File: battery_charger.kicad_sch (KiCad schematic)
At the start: 30 parts, among them J8 Conn_01x04, U15 BQ25895RTW, U17 NX3DV42GU, U18 MP3422GG-P

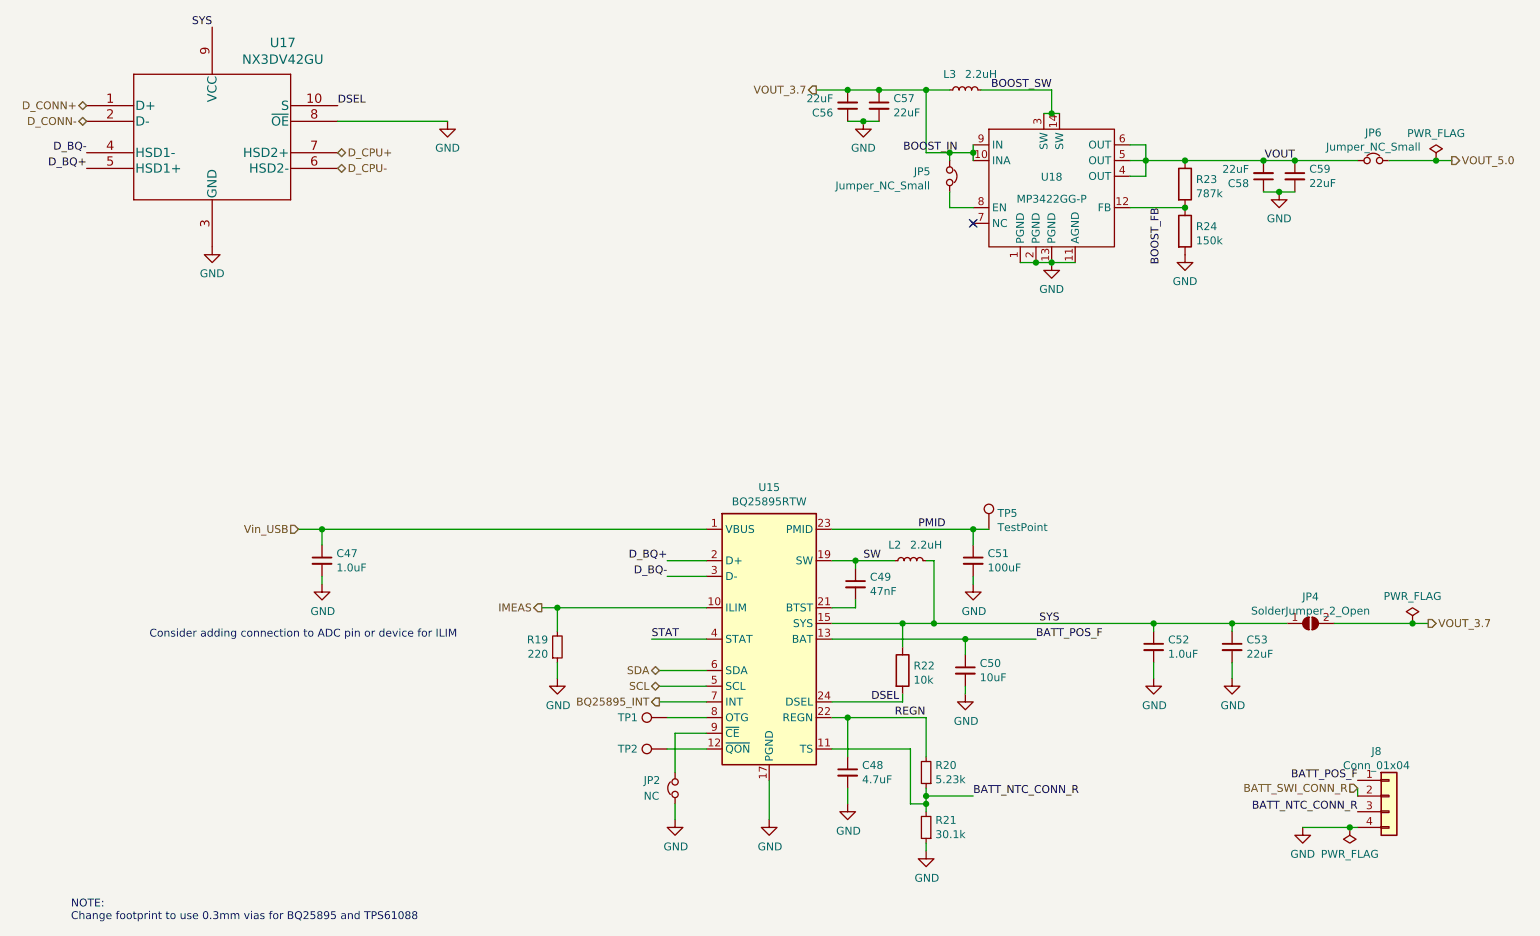
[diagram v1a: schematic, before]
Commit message: Update to Kicad 6.0.0
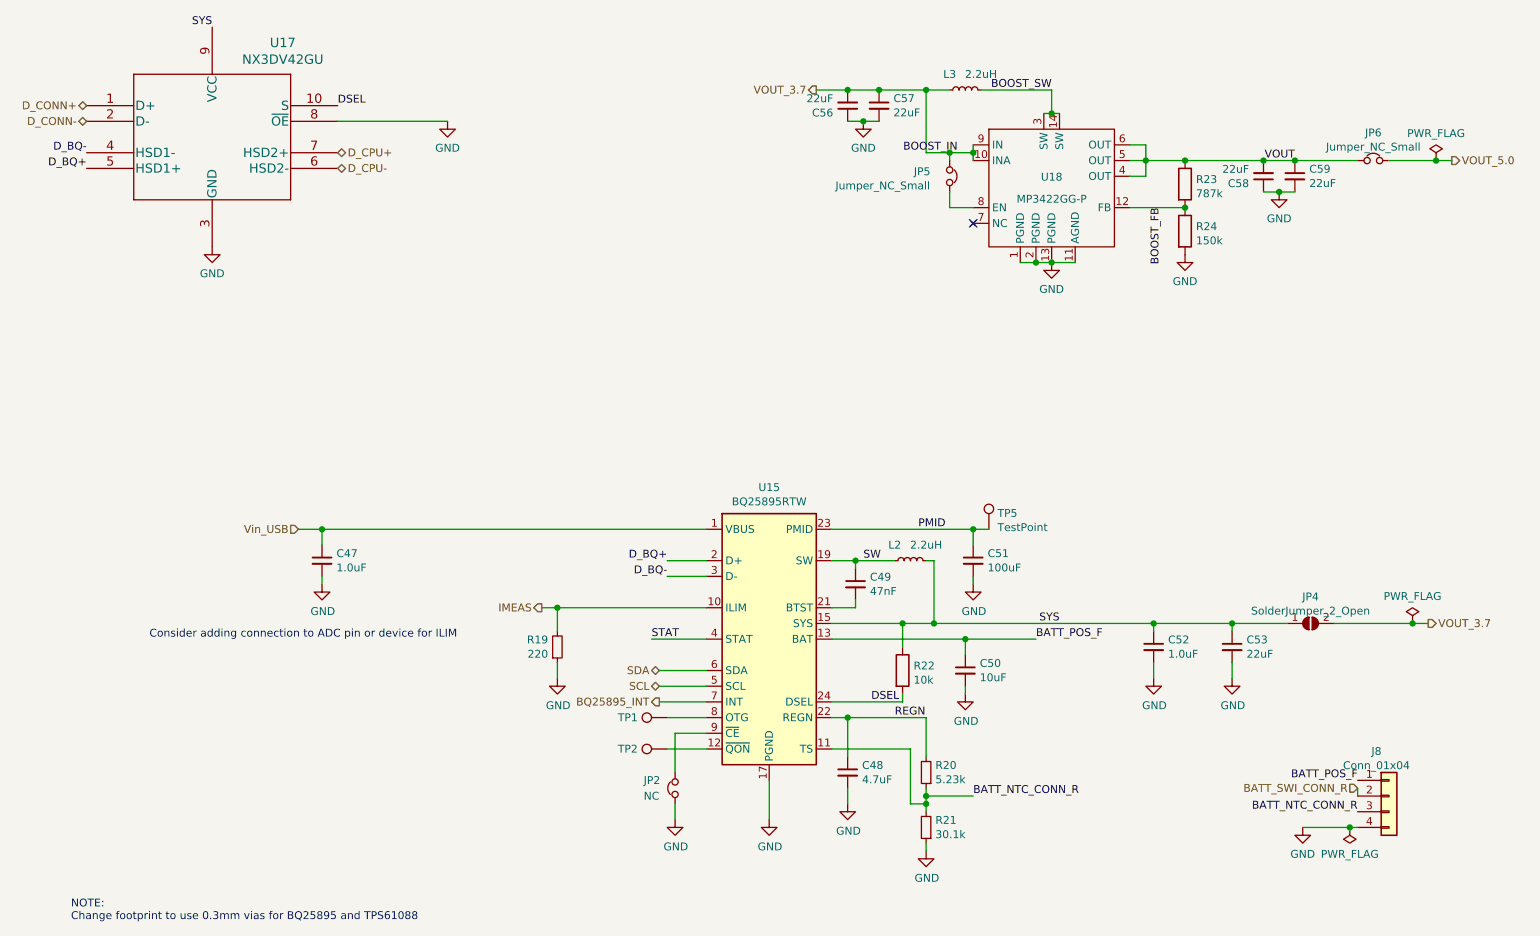
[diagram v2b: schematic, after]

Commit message: Remove tlv320aic3206 and bq25895 and supporting circuitry from schematic; wire up audio/battery connections to Radxa CM3 third connector instead.
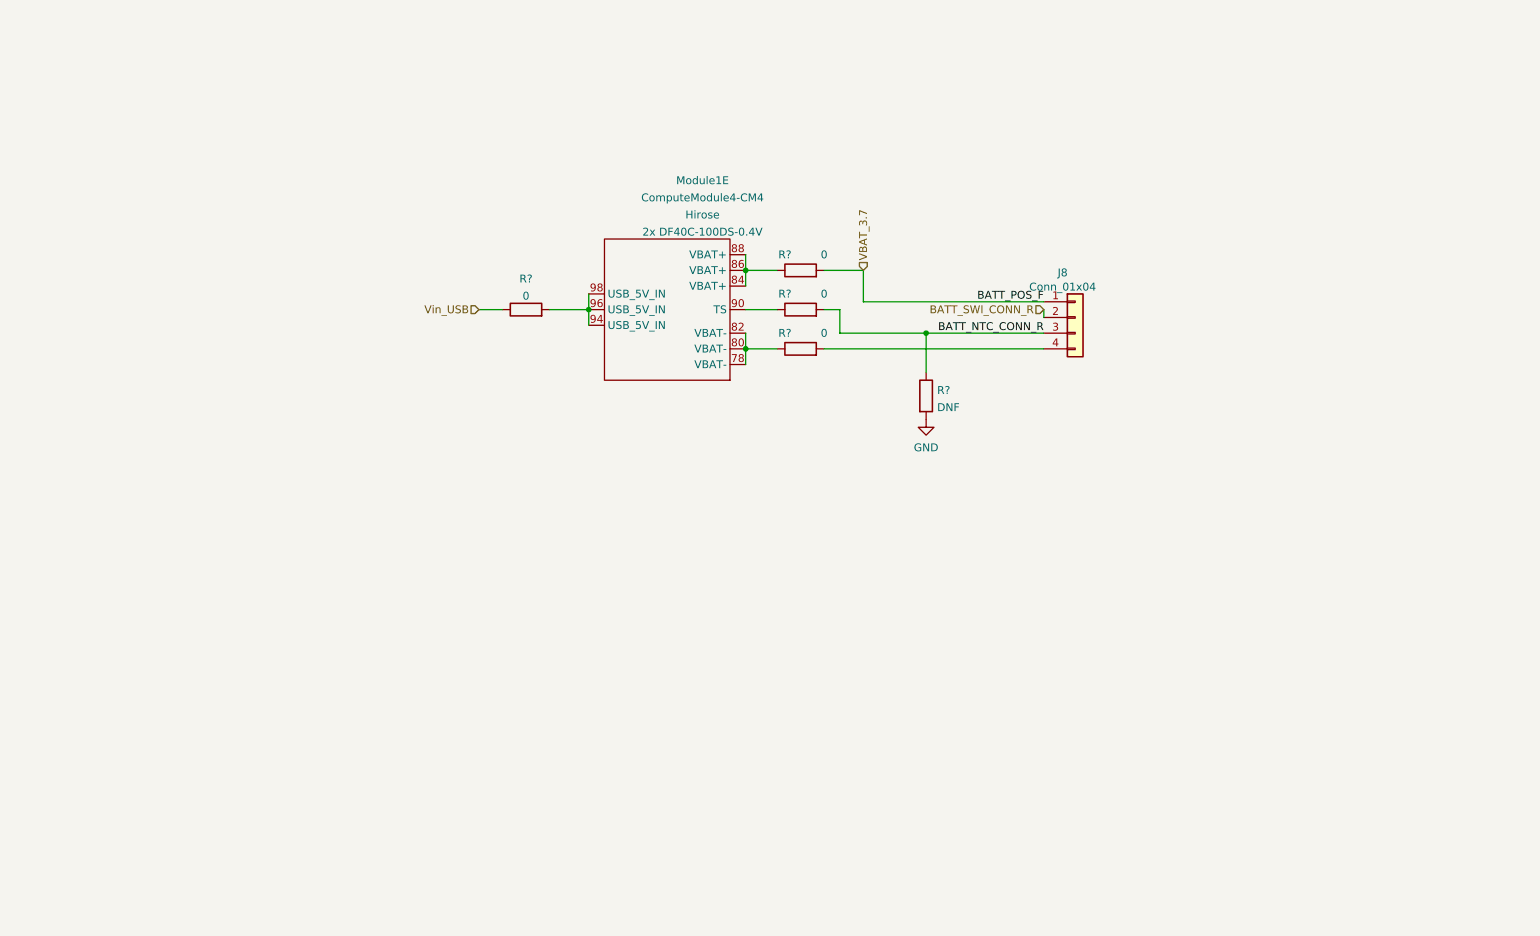
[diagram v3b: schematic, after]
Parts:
- removed C47, C52: 1.0uF, Capacitor_SMD:C_0402_1005Metric, symbol Device:C_Small
- removed C48: 4.7uF, Capacitor_SMD:C_0603_1608Metric, symbol Device:C_Small
- removed C49: 47nF, Capacitor_SMD:C_0402_1005Metric, symbol Device:C_Small
- removed C50: 10uF, Capacitor_SMD:C_0402_1005Metric, symbol Device:C_Small
- removed C51: 100uF, Capacitor_SMD:C_1206_3216Metric, symbol Device:C_Small
- removed C53, C56, C57, C58, C59: 22uF, Capacitor_SMD:C_0805_2012Metric, symbol Device:C_Small
- removed JP2: NC, Resistor_SMD:R_0402_1005Metric, symbol Device:Jumper_NC_Small
- removed JP4: SolderJumper_2_Open, Resistor_SMD:R_0402_1005Metric, symbol Jumper:SolderJumper_2_Open
- removed JP5, JP6: Jumper_NC_Small, Resistor_SMD:R_0402_1005Metric, symbol Device:Jumper_NC_Small
- removed L2, L3: 2.2uH, Inductor_SMD:L_1008_2520Metric, symbol Device:L_Small
- removed R19: 220, Resistor_SMD:R_0402_1005Metric, symbol Device:R_Small
- removed R20: 5.23k, Resistor_SMD:R_0402_1005Metric, symbol Device:R_Small
- removed R21: 30.1k, Resistor_SMD:R_0402_1005Metric, symbol Device:R_Small
- removed R22: 10k, Resistor_SMD:R_0402_1005Metric, symbol Device:R
- removed R23: 787k, Resistor_SMD:R_0402_1005Metric, symbol Device:R
- removed R24: 150k, Resistor_SMD:R_0402_1005Metric, symbol Device:R
- removed TP1, TP2: DNP, TestPoint:TestPoint_Pad_1.0x1.0mm, symbol Connector:TestPoint
- removed TP5: TestPoint, TestPoint:TestPoint_Pad_D1.0mm, symbol Connector:TestPoint
- removed U15: BQ25895RTW, footprints:Texas_S-PWQFN-N24_EP2.7x2.7mm_ThermalVias, symbol Battery_Management:BQ25895RTW
- removed U17: NX3DV42GU, footprints:NX3DV42GU, symbol NX3DV42:NX3DV42GU
- removed U18: MP3422GG-P, footprints:MP3422GG-P, symbol mp3422:MP3422GG-P
- added Module1: ComputeModule4-CM4, CM4IO:Raspberry-Pi-4-Compute-Module, symbol CM4IO:ComputeModule4-CM4
- added R?: DNF, symbol Device:R
- added R? (x4): 0, symbol Device:R
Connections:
- net BATT_NTC_CONN_R: now also R?.1, R?.2
- net GND: now also R?.2; no longer J8.4 (Pin_4)
- net Vin_USB: now also R?.1
- net BATT_POS_F renamed VBAT_3.7
- net VBAT_3.7: now also R?.2
- new net: J8.4 (Pin_4), R?.2
- new net: Module1.78 (VBAT-), Module1.80 (VBAT-), Module1.82 (VBAT-), R?.1
- new net: Module1.84 (VBAT+), Module1.86 (VBAT+), Module1.88 (VBAT+), R?.1
- new net: Module1.94 (USB_5V_IN), Module1.96 (USB_5V_IN), Module1.98 (USB_5V_IN), R?.2
- new net: Module1.90 (TS), R?.1
- no-connect marks 1 -> 0
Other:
- note removed: "Consider adding connection to ADC pin or device for ILIM"
- note removed: "NOTE: Change footprint to use 0.3mm vias for BQ25895 and TPS61088"
- moved on the sheet: J8

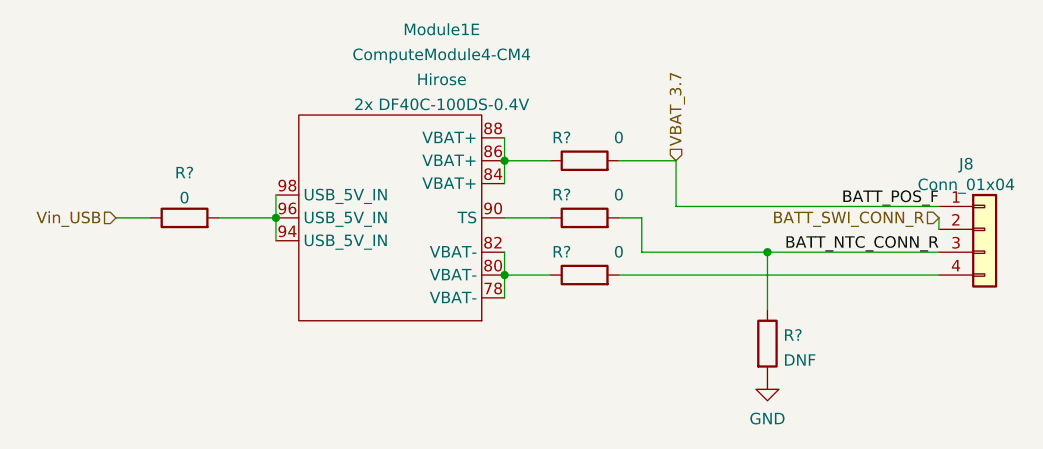
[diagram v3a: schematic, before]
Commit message: Lots of changes to convert to Radxa CM3. Also reroute all the touchscreen connections with smaller tolerances, which avoids having to route anything on inner layers.
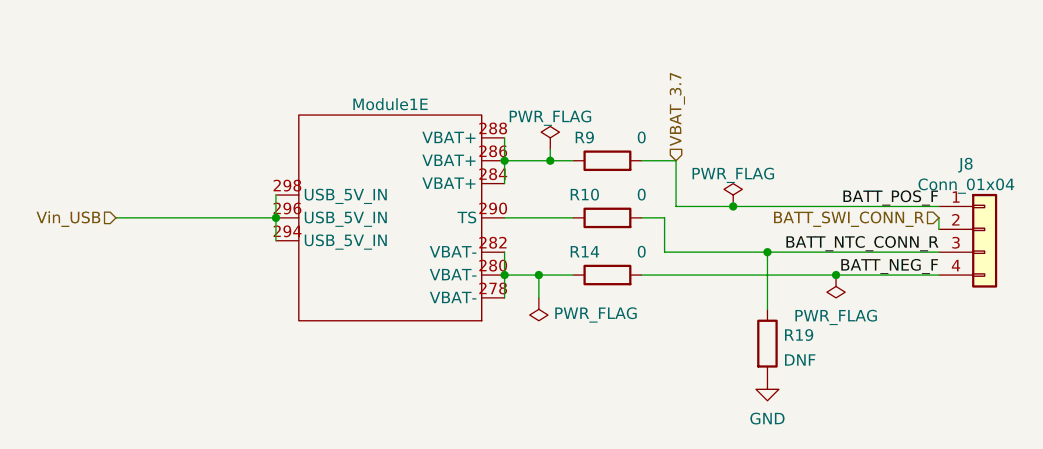
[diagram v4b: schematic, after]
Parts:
- removed R?: 0, symbol Device:R
- Module1: footprint CM4IO:Raspberry-Pi-4-Compute-Module -> footprints:Raspberry-Pi-4-Compute-Module
- R10, R14, R19, R9: renamed from R?; footprint (none) -> Resistor_SMD:R_0402_1005Metric
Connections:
- net Vin_USB: now also Module1.294 (USB_5V_IN), Module1.296 (USB_5V_IN), Module1.298 (USB_5V_IN)
- net BATT_NEG_F: now reaches J8.4 (Pin_4), R14.2
- net at R10.1: now also Module1.290 (TS); no longer Module1.90 (TS)
- new net: Module1.278 (VBAT-), Module1.280 (VBAT-), Module1.282 (VBAT-), R14.1
- new net: Module1.284 (VBAT+), Module1.286 (VBAT+), Module1.288 (VBAT+), R9.1
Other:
- moved on the sheet: R10, R14, R9

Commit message: Final touches on Radxa CM3 version of the board
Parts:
- Module1: value ComputeModule4-CM4 -> Radxa CM3; symbol CM4IO:ComputeModule4-CM4 -> CM4IO:Radxa CM3
- renumbered R9 to JP4, R10 to JP5, R14 to JP6
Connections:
- net VBAT-: now reaches JP6.1, Module1.278 (VBAT-), Module1.280 (VBAT-), Module1.282 (VBAT-)
- net VBAT+: now reaches JP4.1, Module1.284 (VBAT+), Module1.286 (VBAT+), Module1.288 (VBAT+)
- net TS: now reaches JP5.1, Module1.290 (TS)
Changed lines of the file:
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@@
     (stroke (width 0) (type default) (color 0 0 0 0))
   )
-  (wire (pts (xy 144.78 60.96) (xy 144.78 62.23))
+  (wire (pts (xy 144.78 52.07) (xy 144.78 62.23))
     (stroke (width 0) (type default) (color 0 0 0 0))
   )
@@
     (stroke (width 0) (type default) (color 0 0 0 0))
   )
-  (wire (pts (xy 143.51 77.47) (xy 143.51 74.93))
+  (wire (pts (xy 143.51 87.63) (xy 143.51 74.93))
     (stroke (width 0) (type default) (color 0 0 0 0))
   )
@@
     (effects (font (size 1.27 1.27)) (justify right bottom))
   )
+  (label "VBAT+" (at 144.78 58.42 90)
+    (effects (font (size 1.27 1.27)) (justify left bottom))
+  )
+  (label "TS" (at 142.24 68.58 0)
+    (effects (font (size 1.27 1.27)) (justify left bottom))
+  )
+  (label "VBAT-" (at 143.51 83.82 90)
+    (effects (font (size 1.27 1.27)) (justify left bottom))
+  )
   (hierarchical_label "Vin_USB" (shape input) (at 96.52 68.58 180)
     (effects (font (size 1.27 1.27)) (justify right))
@@
     (pin "1")
   )
-  (symbol (lib_id "power:PWR_FLAG") (at 144.78 60.96 0) (unit 1)
-    (in_bom yes) (on_board yes) (fields_autoplaced)
-    (property "Reference" "#FLG0105" (id 0) (at 144.78 59.055 0)
-      (effects (font (size 1.27 1.27)) hide)
-    )
-    (property "Value" "PWR_FLAG" (id 1) (at 144.78 57.3555 0))
-    (property "Footprint" "" (id 2) (at 144.78 60.96 0)
-      (effects (font (size 1.27 1.27)) hide)
-    )
-    (property "Datasheet" "~" (id 3) (at 144.78 60.96 0)
+  (symbol (lib_id "power:PWR_FLAG") (at 144.78 52.07 0) (unit 1)
+    (in_bom yes) (on_board yes) (fields_autoplaced)
+    (property "Reference" "#FLG0105" (id 0) (at 144.78 50.165 0)
+      (effects (font (size 1.27 1.27)) hide)
+    )
+    (property "Value" "PWR_FLAG" (id 1) (at 144.78 48.4655 0))
+    (property "Footprint" "" (id 2) (at 144.78 52.07 0)
+      (effects (font (size 1.27 1.27)) hide)
+    )
+    (property "Datasheet" "~" (id 3) (at 144.78 52.07 0)
       (effects (font (size 1.27 1.27)) hide)
     )
@@
     (pin "1")
   )
-  (symbol (lib_id "power:PWR_FLAG") (at 143.51 77.47 180) (unit 1)
-    (in_bom yes) (on_board yes) (fields_autoplaced)
-    (property "Reference" "#FLG0104" (id 0) (at 143.51 79.375 0)
-      (effects (font (size 1.27 1.27)) hide)
-    )
-    (property "Value" "PWR_FLAG" (id 1) (at 145.161 79.219 0)
+  (symbol (lib_id "power:PWR_FLAG") (at 143.51 87.63 180) (unit 1)
+    (in_bom yes) (on_board yes) (fields_autoplaced)
+    (property "Reference" "#FLG0104" (id 0) (at 143.51 89.535 0)
+      (effects (font (size 1.27 1.27)) hide)
+    )
+    (property "Value" "PWR_FLAG" (id 1) (at 145.161 89.379 0)
       (effects (font (size 1.27 1.27)) (justify right))
     )
-    (property "Footprint" "" (id 2) (at 143.51 77.47 0)
-      (effects (font (size 1.27 1.27)) hide)
-    )
-    (property "Datasheet" "~" (id 3) (at 143.51 77.47 0)
+    (property "Footprint" "" (id 2) (at 143.51 87.63 0)
+      (effects (font (size 1.27 1.27)) hide)
+    )
+    (property "Datasheet" "~" (id 3) (at 143.51 87.63 0)
       (effects (font (size 1.27 1.27)) hide)
     )
@@
   (symbol (lib_id "Device:R") (at 151.13 74.93 90) (unit 1)
     (in_bom yes) (on_board yes)
-    (property "Reference" "R14" (id 0) (at 148.59 72.39 90))
+    (property "Reference" "JP6" (id 0) (at 148.59 72.39 90))
     (property "Value" "0" (id 1) (at 154.94 72.39 90))
     (property "Footprint" "Resistor_SMD:R_0402_1005Metric" (id 2) (at 151.13 76.708 90)
@@
   (symbol (lib_id "Device:R") (at 151.13 62.23 90) (unit 1)
     (in_bom yes) (on_board yes)
-    (property "Reference" "R9" (id 0) (at 148.59 59.69 90))
+    (property "Reference" "JP4" (id 0) (at 148.59 59.69 90))
     (property "Value" "0" (id 1) (at 154.94 59.69 90))
     (property "Footprint" "Resistor_SMD:R_0402_1005Metric" (id 2) (at 151.13 64.008 90)
@@
   (symbol (lib_id "Device:R") (at 151.13 68.58 90) (unit 1)
     (in_bom yes) (on_board yes)
-    (property "Reference" "R10" (id 0) (at 148.59 66.04 90))
+    (property "Reference" "JP5" (id 0) (at 148.59 66.04 90))
     (property "Value" "0" (id 1) (at 154.94 66.04 90))
     (property "Footprint" "Resistor_SMD:R_0402_1005Metric" (id 2) (at 151.13 70.358 90)
@@
     (pin "1")
   )
-  (symbol (lib_id "CM4IO:ComputeModule4-CM4") (at 139.7 90.17 180) (unit 5)
+  (symbol (lib_id "CM4IO:Radxa CM3") (at 139.7 90.17 180) (unit 5)
     (in_bom yes) (on_board yes) (fields_autoplaced)
     (property "Reference" "Module1" (id 0) (at 127 56.0093 0))
-    (property "Value" "ComputeModule4-CM4" (id 1) (at 127 56.0094 0)
+    (property "Value" "Radxa CM3" (id 1) (at 127 56.0094 0)
       (effects (font (size 1.27 1.27)) hide)
     )
@@
       (effects (font (size 1.27 1.27)) hide)
     )
-    (property "Field4" "Hirose" (id 4) (at 127 56.0093 0)
-      (effects (font (size 1.27 1.27)) hide)
-    )
-    (property "Field5" "2x DF40C-100DS-0.4V" (id 5) (at 132.715 56.0094 0)
-      (effects (font (size 1.27 1.27)) hide)
-    )
+    (property "Field4" "Hirose" (id 4) (at 148.59 90.17 0)
+      (effects (font (size 1.27 1.27)) hide)
+    )
+    (property "Field5" "2x DF40C-100DS-0.4V" (id 5) (at 148.59 87.63 0)
+      (effects (font (size 1.27 1.27)) hide)
+    )
